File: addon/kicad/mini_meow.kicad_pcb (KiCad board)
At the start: 2 copper layers, 49.3 x 63.4 mm, 13 parts, among them U1 sa_connector

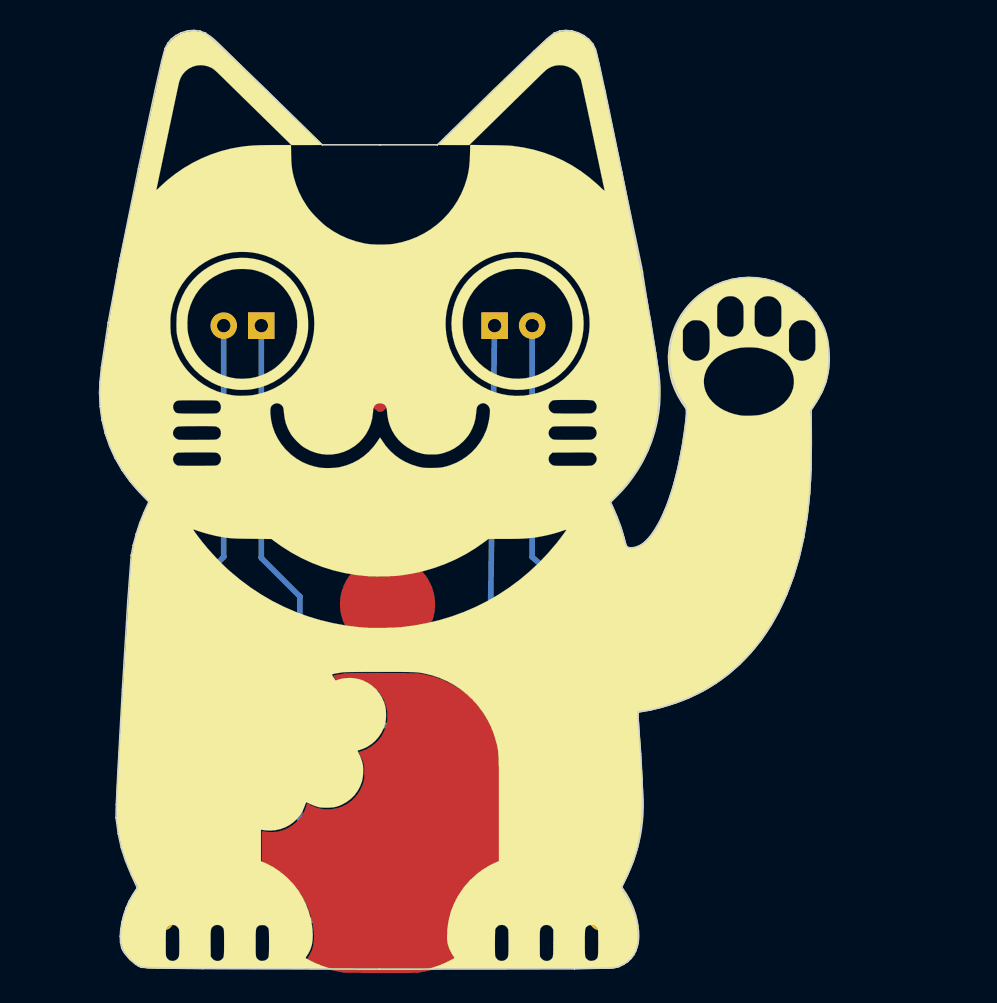
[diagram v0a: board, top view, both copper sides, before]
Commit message: created SAO Rev2 with correct connector orientation
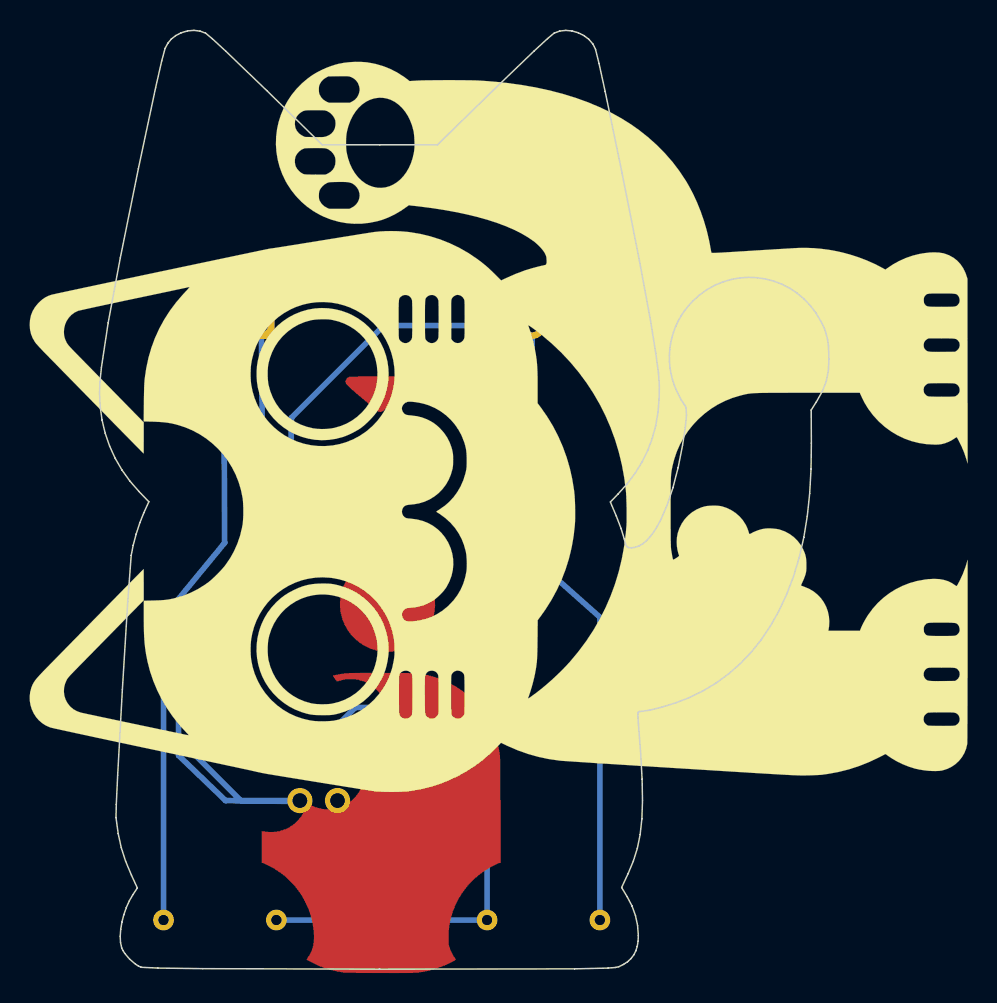
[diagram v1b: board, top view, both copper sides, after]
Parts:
- moved G*** 1.41 mm to (153.0, 89.9), turned to 90 degrees
- turned U1 to 270 degrees
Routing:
- net GND: track 67.9 -> 90.4 mm
- net +3V3: track 25.6 -> 40.5 mm
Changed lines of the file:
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@@
     (links 6)
     (no_connects 0)
-    (area 129.545923 60.619632 179.358787 124.739737)
+    (area 124.818132 60.787309 188.661475 124.739737)
     (thickness 1.6)
     (drawings 228)
-    (tracks 20)
+    (tracks 28)
     (zones 0)
     (modules 13)
@@
   (page A4)
   (layers
-    (0 F.Cu signal)
+    (0 F.Cu signal hide)
     (31 B.Cu signal)
-    (32 B.Adhes user)
-    (33 F.Adhes user)
-    (34 B.Paste user)
-    (35 F.Paste user)
+    (32 B.Adhes user hide)
+    (33 F.Adhes user hide)
+    (34 B.Paste user hide)
+    (35 F.Paste user hide)
     (36 B.SilkS user)
-    (37 F.SilkS user)
-    (38 B.Mask user)
-    (39 F.Mask user)
-    (40 Dwgs.User user)
+    (37 F.SilkS user hide)
+    (38 B.Mask user hide)
+    (39 F.Mask user hide)
+    (40 Dwgs.User user hide)
     (41 Cmts.User user)
     (42 Eco1.User user)
@@
     (visible_elements FFFFFF7F)
     (pcbplotparams
-      (layerselection 0x00030_80000001)
-      (usegerberextensions false)
+      (layerselection 0x011f0_80000001)
+      (usegerberextensions true)
       (excludeedgelayer true)
       (linewidth 0.100000)
@@
       (outputformat 1)
       (mirror false)
-      (drillshape 1)
+      (drillshape 0)
       (scaleselection 1)
-      (outputdirectory ""))
+      (outputdirectory gerber_rev2/))
   )
   (net 0 "")
@@
   )
   (module Pin_Headers:Pin_Header_Straight_2x02_Pitch2.54mm (layer B.Cu)
-    (at 143.3195 110.2995 90)
+    (at 143.3195 110.2995 270)
     (descr "Through hole straight pin header, 2x02, 2.54mm pitch, double rows")
     (tags "Through hole pin header THT 2x02 2.54mm double row")
-    (fp_text reference U1 (at 1.27 2.33 90) (layer B.SilkS)
+    (fp_text reference U1 (at 1.27 2.33 270) (layer B.SilkS)
       (effects (font (size 1 1) (thickness 0.15)) (justify mirror))
     )
-    (fp_text value sa_connector (at 1.27 -4.87 90) (layer B.Fab)
+    (fp_text value sa_connector (at 2.159 -5.0165 450) (layer B.Fab)
       (effects (font (size 1 1) (thickness 0.15)) (justify mirror))
     )
@@
     (fp_line (start 4.35 -4.35) (end 4.35 1.8) (layer B.CrtYd) (width 0.05))
     (fp_line (start 4.35 1.8) (end -1.8 1.8) (layer B.CrtYd) (width 0.05))
-    (fp_text user %R (at 1.27 -1.27 360) (layer B.Fab)
+    (fp_text user %R (at 1.27 -1.27 540) (layer B.Fab)
       (effects (font (size 1 1) (thickness 0.15)) (justify mirror))
     )
-    (pad 1 thru_hole rect (at 0 0 90) (size 1.7 1.7) (drill 1) (layers *.Cu *.Mask)
+    (pad 1 thru_hole rect (at 0 0 270) (size 1.7 1.7) (drill 1) (layers *.Cu *.Mask)
       (net 4 +3V3))
-    (pad 2 thru_hole oval (at 2.54 0 90) (size 1.7 1.7) (drill 1) (layers *.Cu *.Mask)
+    (pad 2 thru_hole oval (at 2.54 0 270) (size 1.7 1.7) (drill 1) (layers *.Cu *.Mask)
       (net 1 GND))
-    (pad 3 thru_hole oval (at 0 -2.54 90) (size 1.7 1.7) (drill 1) (layers *.Cu *.Mask)
+    (pad 3 thru_hole oval (at 0 -2.54 270) (size 1.7 1.7) (drill 1) (layers *.Cu *.Mask)
       (net 5 "Net-(U1-Pad3)"))
-    (pad 4 thru_hole oval (at 2.54 -2.54 90) (size 1.7 1.7) (drill 1) (layers *.Cu *.Mask)
+    (pad 4 thru_hole oval (at 2.54 -2.54 270) (size 1.7 1.7) (drill 1) (layers *.Cu *.Mask)
       (net 6 "Net-(U1-Pad4)"))
     (model ${KISYS3DMOD}/Pin_Headers.3dshapes/Pin_Header_Straight_2x02_Pitch2.54mm.wrl
@@
   )
   (module mini_meow:mini_meow_silk_lg (layer F.Cu)
-    (at 152.146 88.773)
-    (fp_text reference G*** (at 0 0) (layer F.SilkS) hide
+    (at 152.9715 89.916 90)
+    (fp_text reference G*** (at 0 0 90) (layer F.SilkS) hide
       (effects (font (thickness 0.3)))
     )
-    (fp_text value LOGO (at 0.75 0) (layer F.SilkS) hide
+    (fp_text value LOGO (at 0.75 0 90) (layer F.SilkS) hide
       (effects (font (thickness 0.3)))
     )
@@
     (effects (font (size 1 1) (thickness 0.2)) (justify mirror))
   )
-  (gr_text VCC (at 147.066 112.7125) (layer B.SilkS)
+  (gr_text VCC (at 143.0655 107.569) (layer B.SilkS)
     (effects (font (size 1 1) (thickness 0.2)) (justify mirror))
   )
-  (gr_text GND (at 147.2565 106.2355) (layer B.SilkS)
+  (gr_text GND (at 143.764 115.57) (layer B.SilkS)
     (effects (font (size 1 1) (thickness 0.2)) (justify mirror))
   )
@@
   (gr_line (start 132.41897 124.01002) (end 132.220026 123.884121) (layer Edge.Cuts) (width 0.1))
   (gr_line (start 132.607035 124.095547) (end 132.41897 124.01002) (layer Edge.Cuts) (width 0.1))
-  (segment (start 156.464 80.772) (end 156.083 107.823) (width 0.381) (layer B.Cu) (net 1))
-  (segment (start 145.161 107.7595) (end 143.3195 107.7595) (width 0.381) (layer B.Cu) (net 1))
-  (segment (start 156.083 107.823) (end 145.161 107.7595) (width 0.381) (layer B.Cu) (net 1))
-  (segment (start 140.716 80.772) (end 140.716 96.4565) (width 0.381) (layer B.Cu) (net 1))
-  (segment (start 143.3195 99.06) (end 143.3195 107.7595) (width 0.381) (layer B.Cu) (net 1))
-  (segment (start 140.716 96.4565) (end 143.3195 99.06) (width 0.381) (layer B.Cu) (net 1))
+  (segment (start 148.971 80.772) (end 148.971 80.772) (width 0.381) (layer B.Cu) (net 1))
+  (segment (start 156.464 80.772) (end 148.971 80.772) (width 0.381) (layer B.Cu) (net 1) (status 400000))
+  (segment (start 142.746876 86.996124) (end 148.971 80.772) (width 0.381) (layer B.Cu) (net 1))
+  (segment (start 143.3195 112.8395) (end 139.319 112.8395) (width 0.381) (layer B.Cu) (net 1))
+  (segment (start 142.6845 94.6785) (end 142.746876 86.996124) (width 0.381) (layer B.Cu) (net 1))
+  (segment (start 136.271 101.981) (end 142.6845 94.6785) (width 0.381) (layer B.Cu) (net 1))
+  (segment (start 136.271 109.7915) (end 136.271 101.981) (width 0.381) (layer B.Cu) (net 1))
+  (segment (start 139.319 112.8395) (end 136.271 109.7915) (width 0.381) (layer B.Cu) (net 1))
+  (segment (start 138.303 112.8395) (end 143.3195 112.903) (width 0.381) (layer B.Cu) (net 1))
+  (segment (start 135.128 109.7915) (end 138.303 112.8395) (width 0.381) (layer B.Cu) (net 1))
+  (segment (start 135.128 101.092) (end 135.128 109.7915) (width 0.381) (layer B.Cu) (net 1))
+  (segment (start 140.843 94.742) (end 135.128 101.092) (width 0.381) (layer B.Cu) (net 1))
+  (segment (start 140.716 80.772) (end 140.843 94.742) (width 0.381) (layer B.Cu) (net 1))
   (segment (start 159.004 80.772) (end 159.004 96.393) (width 0.381) (layer B.Cu) (net 2))
   (segment (start 163.576 100.457) (end 163.576 120.904) (width 0.381) (layer B.Cu) (net 2))
   (segment (start 159.004 96.393) (end 163.576 100.457) (width 0.381) (layer B.Cu) (net 2))
   (segment (start 134.112 120.904) (end 134.112 100.457) (width 0.381) (layer B.Cu) (net 3))
-  (segment (start 138.176 96.393) (end 138.176 80.772) (width 0.381) (layer B.Cu) (net 3))
-  (segment (start 134.112 100.457) (end 138.176 96.393) (width 0.381) (layer B.Cu) (net 3))
-  (segment (start 143.3195 110.2995) (end 143.3195 117.348) (width 0.381) (layer B.Cu) (net 4))
-  (segment (start 141.7955 118.872) (end 141.7955 120.8405) (width 0.381) (layer B.Cu) (net 4))
-  (segment (start 143.3195 117.348) (end 141.7955 118.872) (width 0.381) (layer B.Cu) (net 4))
+  (segment (start 138.2395 95.4405) (end 138.176 80.772) (width 0.381) (layer B.Cu) (net 3))
+  (segment (start 134.112 100.457) (end 138.2395 95.4405) (width 0.381) (layer B.Cu) (net 3))
+  (segment (start 155.956 120.904) (end 155.956 110.744) (width 0.381) (layer B.Cu) (net 4))
+  (segment (start 147.066 106.553) (end 143.3195 110.2995) (width 0.381) (layer B.Cu) (net 4))
+  (segment (start 151.765 106.553) (end 147.066 106.553) (width 0.381) (layer B.Cu) (net 4))
+  (segment (start 155.956 110.744) (end 151.765 106.553) (width 0.381) (layer B.Cu) (net 4))
   (segment (start 141.7955 120.8405) (end 141.732 120.904) (width 0.381) (layer B.Cu) (net 4))
   (segment (start 155.956 120.904) (end 155.956 120.777) (width 0.381) (layer B.Cu) (net 4))
